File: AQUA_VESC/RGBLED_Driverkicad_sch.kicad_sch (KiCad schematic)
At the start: 12 parts, among them Q10 AO3400A, Q11 AO3401A, Q12 AO3400A, Q13 AO3401A, Q8 AO3400A, Q9 AO3401A

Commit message: AQUA VESC仮完成
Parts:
- renumbered R85 to R84, R86 to R85, R87 to R86, R88 to R87, R89 to R88, R90 to R89
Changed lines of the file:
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@@
 		(dnp no)
 		(fields_autoplaced yes)
-		(property "Reference" "#PWR0123"
+		(property "Reference" "#PWR0112"
 			(at 128.27 77.47 0)
 			(effects
@@
 			(project "AQUA_VESC"
 				(path "/8ee9fd02-9bd5-4905-927f-d8ca1179f479/3e003488-3a27-47f4-bde4-f49a514f4d8a"
-					(reference "#PWR0123")
+					(reference "#PWR0112")
 					(unit 1)
 				)
@@
 		(dnp no)
 		(fields_autoplaced yes)
-		(property "Reference" "#PWR0121"
+		(property "Reference" "#PWR0109"
 			(at 82.55 77.47 0)
 			(effects
@@
 			(project "AQUA_VESC"
 				(path "/8ee9fd02-9bd5-4905-927f-d8ca1179f479/3e003488-3a27-47f4-bde4-f49a514f4d8a"
-					(reference "#PWR0121")
+					(reference "#PWR0109")
 					(unit 1)
 				)
@@
 		(dnp no)
 		(fields_autoplaced yes)
-		(property "Reference" "R85"
+		(property "Reference" "R84"
 			(at 43.18 63.4999 0)
 			(effects
@@
 			(project "AQUA_VESC"
 				(path "/8ee9fd02-9bd5-4905-927f-d8ca1179f479/3e003488-3a27-47f4-bde4-f49a514f4d8a"
-					(reference "R85")
+					(reference "R84")
 					(unit 1)
 				)
@@
 		(dnp no)
 		(fields_autoplaced yes)
-		(property "Reference" "R88"
+		(property "Reference" "R87"
 			(at 92.71 44.4499 0)
 			(effects
@@
 			(project "AQUA_VESC"
 				(path "/8ee9fd02-9bd5-4905-927f-d8ca1179f479/3e003488-3a27-47f4-bde4-f49a514f4d8a"
-					(reference "R88")
+					(reference "R87")
 					(unit 1)
 				)
@@
 		(dnp no)
 		(fields_autoplaced yes)
-		(property "Reference" "#PWR0113"
+		(property "Reference" "#PWR0107"
 			(at 48.26 41.91 0)
 			(effects
@@
 			(project "AQUA_VESC"
 				(path "/8ee9fd02-9bd5-4905-927f-d8ca1179f479/3e003488-3a27-47f4-bde4-f49a514f4d8a"
-					(reference "#PWR0113")
+					(reference "#PWR0107")
 					(unit 1)
 				)
@@
 		(dnp no)
 		(fields_autoplaced yes)
-		(property "Reference" "#PWR0117"
+		(property "Reference" "#PWR0111"
 			(at 90.17 77.47 0)
 			(effects
@@
 			(project "AQUA_VESC"
 				(path "/8ee9fd02-9bd5-4905-927f-d8ca1179f479/3e003488-3a27-47f4-bde4-f49a514f4d8a"
-					(reference "#PWR0117")
+					(reference "#PWR0111")
 					(unit 1)
 				)
@@
 		(dnp no)
 		(fields_autoplaced yes)
-		(property "Reference" "#PWR0120"
+		(property "Reference" "#PWR0114"
 			(at 135.89 77.47 0)
 			(effects
@@
 			(project "AQUA_VESC"
 				(path "/8ee9fd02-9bd5-4905-927f-d8ca1179f479/3e003488-3a27-47f4-bde4-f49a514f4d8a"
-					(reference "#PWR0120")
+					(reference "#PWR0114")
 					(unit 1)
 				)
@@
 		(dnp no)
 		(fields_autoplaced yes)
-		(property "Reference" "#PWR0122"
+		(property "Reference" "#PWR0106"
 			(at 40.64 76.2 0)
 			(effects
@@
 			(project "AQUA_VESC"
 				(path "/8ee9fd02-9bd5-4905-927f-d8ca1179f479/3e003488-3a27-47f4-bde4-f49a514f4d8a"
-					(reference "#PWR0122")
+					(reference "#PWR0106")
 					(unit 1)
 				)
@@
 		(dnp no)
 		(fields_autoplaced yes)
-		(property "Reference" "#PWR0114"
+		(property "Reference" "#PWR0108"
 			(at 48.26 76.2 0)
 			(effects
@@
 			(project "AQUA_VESC"
 				(path "/8ee9fd02-9bd5-4905-927f-d8ca1179f479/3e003488-3a27-47f4-bde4-f49a514f4d8a"
-					(reference "#PWR0114")
+					(reference "#PWR0108")
 					(unit 1)
 				)
@@
 		(dnp no)
 		(fields_autoplaced yes)
-		(property "Reference" "R86"
+		(property "Reference" "R85"
 			(at 50.8 43.1799 0)
 			(effects
@@
 			(project "AQUA_VESC"
 				(path "/8ee9fd02-9bd5-4905-927f-d8ca1179f479/3e003488-3a27-47f4-bde4-f49a514f4d8a"
-					(reference "R86")
+					(reference "R85")
 					(unit 1)
 				)
@@
 		(dnp no)
 		(fields_autoplaced yes)
-		(property "Reference" "R89"
+		(property "Reference" "R88"
 			(at 130.81 64.7699 0)
 			(effects
@@
 			(project "AQUA_VESC"
 				(path "/8ee9fd02-9bd5-4905-927f-d8ca1179f479/3e003488-3a27-47f4-bde4-f49a514f4d8a"
-					(reference "R89")
+					(reference "R88")
 					(unit 1)
 				)
@@
 		(dnp no)
 		(fields_autoplaced yes)
-		(property "Reference" "#PWR0119"
+		(property "Reference" "#PWR0113"
 			(at 135.89 43.18 0)
 			(effects
@@
 			(project "AQUA_VESC"
 				(path "/8ee9fd02-9bd5-4905-927f-d8ca1179f479/3e003488-3a27-47f4-bde4-f49a514f4d8a"
-					(reference "#PWR0119")
+					(reference "#PWR0113")
 					(unit 1)
 				)
@@
 		(dnp no)
 		(fields_autoplaced yes)
-		(property "Reference" "R90"
+		(property "Reference" "R89"
 			(at 138.43 44.4499 0)
 			(effects
@@
 			(project "AQUA_VESC"
 				(path "/8ee9fd02-9bd5-4905-927f-d8ca1179f479/3e003488-3a27-47f4-bde4-f49a514f4d8a"
-					(reference "R90")
+					(reference "R89")
 					(unit 1)
 				)
@@
 		(dnp no)
 		(fields_autoplaced yes)
-		(property "Reference" "R87"
+		(property "Reference" "R86"
 			(at 85.09 64.7699 0)
 			(effects
@@
 			(project "AQUA_VESC"
 				(path "/8ee9fd02-9bd5-4905-927f-d8ca1179f479/3e003488-3a27-47f4-bde4-f49a514f4d8a"
-					(reference "R87")
+					(reference "R86")
 					(unit 1)
 				)
@@
 		(dnp no)
 		(fields_autoplaced yes)
-		(property "Reference" "#PWR0116"
+		(property "Reference" "#PWR0110"
 			(at 90.17 43.18 0)
 			(effects
@@
 			(project "AQUA_VESC"
 				(path "/8ee9fd02-9bd5-4905-927f-d8ca1179f479/3e003488-3a27-47f4-bde4-f49a514f4d8a"
-					(reference "#PWR0116")
-					(unit 1)
-				)
+					(reference "#PWR0110")
+					(unit 1)
+				)

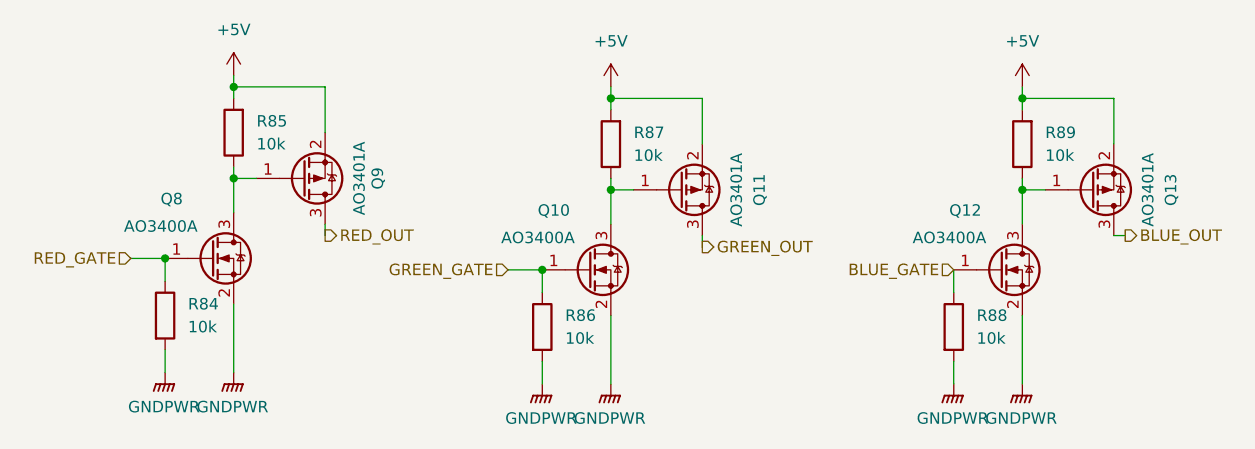
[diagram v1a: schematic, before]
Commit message: AQUA_VESC REV01作成
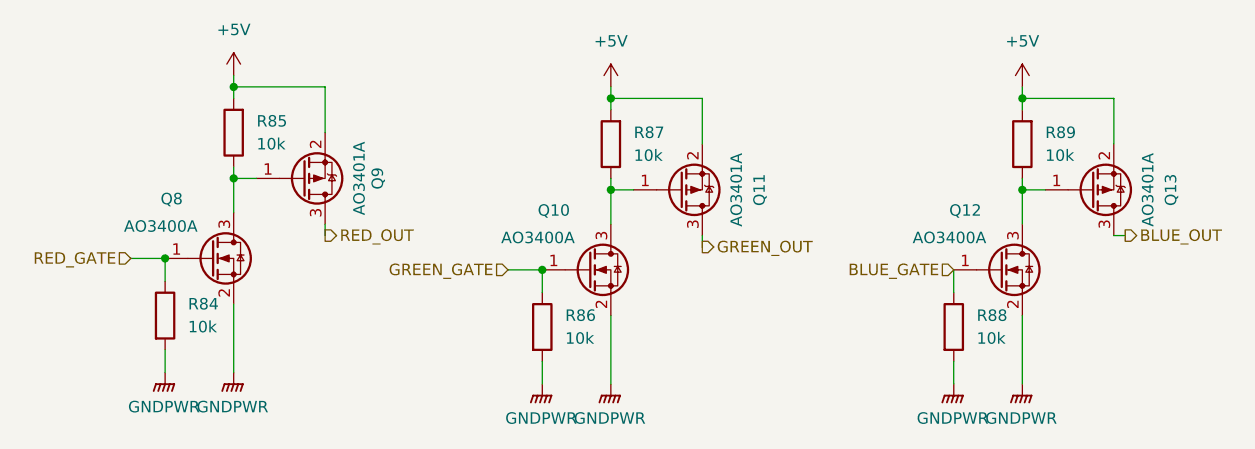
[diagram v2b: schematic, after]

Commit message: 制御基板REV01完成
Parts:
- removed Q10, Q12, Q8: AO3400A, Package_TO_SOT_SMD:SOT-23, symbol Transistor_FET:AO3400A
- added Q11, Q7, Q9: 2N7002, Package_TO_SOT_SMD:SOT-23, symbol Transistor_FET:2N7002
- renumbered Q11 to Q10, Q13 to Q12, Q9 to Q8, R84 to R68, R85 to R69, R86 to R70, R87 to R71, R88 to R72, R89 to R73
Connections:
- net BLUE_GATE: now also Q11.1 (G)
- net GNDPWR: now also Q11.2 (S), Q7.2 (S), Q9.2 (S)
- net GREEN_GATE: now also Q9.1 (G)
- net RED_GATE: now also Q7.1 (G)
- net at Q12.1 (G), R73.1: now also Q11.3 (D)
- net at Q10.1 (G), R71.1: now also Q9.3 (D)
- net at Q8.1 (G), R69.1: now also Q7.3 (D)

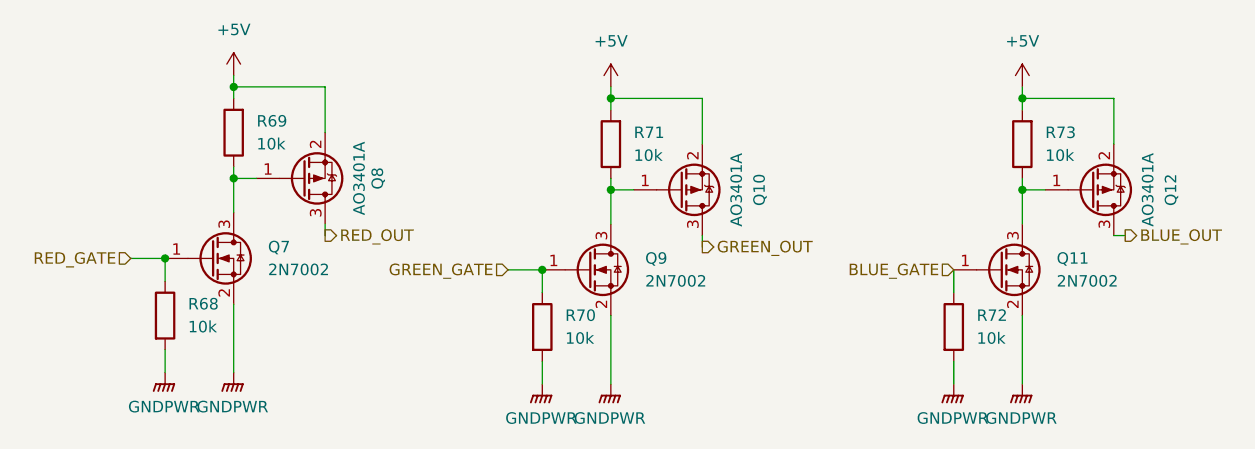
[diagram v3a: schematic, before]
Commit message: 方針変更、back_connector_escにMT60を使用しないことに
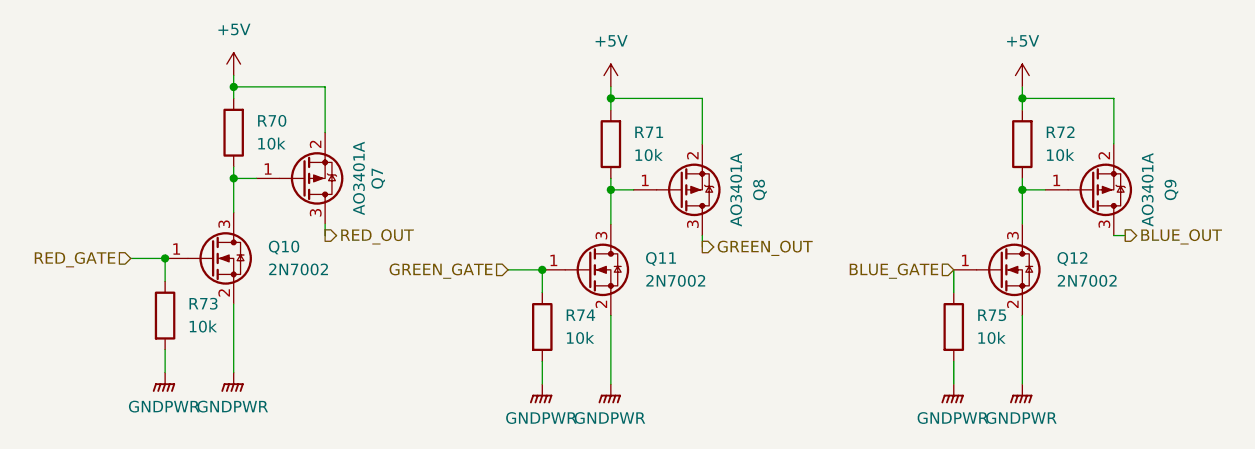
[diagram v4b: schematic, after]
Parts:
- renumbered Q7 to Q10, Q9 to Q11, Q11 to Q12, Q8 to Q7, Q10 to Q8, Q12 to Q9, R69 to R70, R73 to R72, R68 to R73, R70 to R74, R72 to R75
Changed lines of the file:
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@@
 		(on_board yes)
 		(dnp no)
-		(property "Reference" "Q12"
+		(property "Reference" "Q9"
 			(at 152.4 50.8 90)
 			(effects
@@
 			(project "AQUA_VESC"
 				(path "/8ee9fd02-9bd5-4905-927f-d8ca1179f479/3e003488-3a27-47f4-bde4-f49a514f4d8a"
-					(reference "Q12")
+					(reference "Q9")
 					(unit 1)
 				)
@@
 		(dnp no)
 		(fields_autoplaced yes)
-		(property "Reference" "#PWR095"
+		(property "Reference" "#PWR0102"
 			(at 128.27 77.47 0)
 			(effects
@@
 			(project "AQUA_VESC"
 				(path "/8ee9fd02-9bd5-4905-927f-d8ca1179f479/3e003488-3a27-47f4-bde4-f49a514f4d8a"
-					(reference "#PWR095")
+					(reference "#PWR0102")
 					(unit 1)
 				)
@@
 		(dnp no)
 		(fields_autoplaced yes)
-		(property "Reference" "Q7"
+		(property "Reference" "Q10"
 			(at 52.07 57.1499 0)
 			(effects
@@
 			(project ""
 				(path "/8ee9fd02-9bd5-4905-927f-d8ca1179f479/3e003488-3a27-47f4-bde4-f49a514f4d8a"
-					(reference "Q7")
+					(reference "Q10")
 					(unit 1)
 				)
@@
 		(dnp no)
 		(fields_autoplaced yes)
-		(property "Reference" "#PWR092"
+		(property "Reference" "#PWR0100"
 			(at 82.55 77.47 0)
 			(effects
@@
 			(project "AQUA_VESC"
 				(path "/8ee9fd02-9bd5-4905-927f-d8ca1179f479/3e003488-3a27-47f4-bde4-f49a514f4d8a"
-					(reference "#PWR092")
+					(reference "#PWR0100")
 					(unit 1)
 				)
@@
 		(dnp no)
 		(fields_autoplaced yes)
-		(property "Reference" "Q9"
+		(property "Reference" "Q11"
 			(at 93.98 58.4199 0)
 			(effects
@@
 			(project "AQUA_VESC"
 				(path "/8ee9fd02-9bd5-4905-927f-d8ca1179f479/3e003488-3a27-47f4-bde4-f49a514f4d8a"
-					(reference "Q9")
+					(reference "Q11")
 					(unit 1)
 				)
@@
 		(dnp no)
 		(fields_autoplaced yes)
-		(property "Reference" "R68"
+		(property "Reference" "R73"
 			(at 43.18 63.4999 0)
 			(effects
@@
 			(project "AQUA_VESC"
 				(path "/8ee9fd02-9bd5-4905-927f-d8ca1179f479/3e003488-3a27-47f4-bde4-f49a514f4d8a"
-					(reference "R68")
+					(reference "R73")
 					(unit 1)
 				)
@@
 		(dnp no)
 		(fields_autoplaced yes)
-		(property "Reference" "#PWR090"
+		(property "Reference" "#PWR095"
 			(at 48.26 41.91 0)
 			(effects
@@
 			(project "AQUA_VESC"
 				(path "/8ee9fd02-9bd5-4905-927f-d8ca1179f479/3e003488-3a27-47f4-bde4-f49a514f4d8a"
-					(reference "#PWR090")
+					(reference "#PWR095")
 					(unit 1)
 				)
@@
 		(dnp no)
 		(fields_autoplaced yes)
-		(property "Reference" "#PWR094"
+		(property "Reference" "#PWR0101"
 			(at 90.17 77.47 0)
 			(effects
@@
 			(project "AQUA_VESC"
 				(path "/8ee9fd02-9bd5-4905-927f-d8ca1179f479/3e003488-3a27-47f4-bde4-f49a514f4d8a"
-					(reference "#PWR094")
+					(reference "#PWR0101")
 					(unit 1)
 				)
@@
 		(dnp no)
 		(fields_autoplaced yes)
-		(property "Reference" "#PWR097"
+		(property "Reference" "#PWR0103"
 			(at 135.89 77.47 0)
 			(effects
@@
 			(project "AQUA_VESC"
 				(path "/8ee9fd02-9bd5-4905-927f-d8ca1179f479/3e003488-3a27-47f4-bde4-f49a514f4d8a"
-					(reference "#PWR097")
+					(reference "#PWR0103")
 					(unit 1)
 				)
@@
 		(dnp no)
 		(fields_autoplaced yes)
-		(property "Reference" "#PWR089"
+		(property "Reference" "#PWR098"
 			(at 40.64 76.2 0)
 			(effects
@@
 			(project "AQUA_VESC"
 				(path "/8ee9fd02-9bd5-4905-927f-d8ca1179f479/3e003488-3a27-47f4-bde4-f49a514f4d8a"
-					(reference "#PWR089")
+					(reference "#PWR098")
 					(unit 1)
 				)
@@
 		(dnp no)
 		(fields_autoplaced yes)
-		(property "Reference" "#PWR091"
+		(property "Reference" "#PWR099"
 			(at 48.26 76.2 0)
 			(effects
@@
 			(project "AQUA_VESC"
 				(path "/8ee9fd02-9bd5-4905-927f-d8ca1179f479/3e003488-3a27-47f4-bde4-f49a514f4d8a"
-					(reference "#PWR091")
+					(reference "#PWR099")
 					(unit 1)
 				)
@@
 		(dnp no)
 		(fields_autoplaced yes)
-		(property "Reference" "Q11"
+		(property "Reference" "Q12"
 			(at 139.7 58.4199 0)
 			(effects
@@
 			(project "AQUA_VESC"
 				(path "/8ee9fd02-9bd5-4905-927f-d8ca1179f479/3e003488-3a27-47f4-bde4-f49a514f4d8a"
-					(reference "Q11")
+					(reference "Q12")
 					(unit 1)
 				)
@@
 		(dnp no)
 		(fields_autoplaced yes)
-		(property "Reference" "R69"
+		(property "Reference" "R70"
 			(at 50.8 43.1799 0)
 			(effects
@@
 			(project "AQUA_VESC"
 				(path "/8ee9fd02-9bd5-4905-927f-d8ca1179f479/3e003488-3a27-47f4-bde4-f49a514f4d8a"
-					(reference "R69")
+					(reference "R70")
 					(unit 1)
 				)
@@
 		(dnp no)
 		(fields_autoplaced yes)
-		(property "Reference" "R72"
+		(property "Reference" "R75"
 			(at 130.81 64.7699 0)
 			(effects
@@
 			(project "AQUA_VESC"
 				(path "/8ee9fd02-9bd5-4905-927f-d8ca1179f479/3e003488-3a27-47f4-bde4-f49a514f4d8a"
-					(reference "R72")
+					(reference "R75")
 					(unit 1)
 				)
@@
 		(on_board yes)
 		(dnp no)
-		(property "Reference" "Q10"
+		(property "Reference" "Q8"
 			(at 106.68 50.8 90)
 			(effects
@@
 			(project "AQUA_VESC"
 				(path "/8ee9fd02-9bd5-4905-927f-d8ca1179f479/3e003488-3a27-47f4-bde4-f49a514f4d8a"
-					(reference "Q10")
+					(reference "Q8")
 					(unit 1)
 				)
@@
 		(dnp no)
 		(fields_autoplaced yes)
-		(property "Reference" "#PWR096"
+		(property "Reference" "#PWR097"
 			(at 135.89 43.18 0)
 			(effects
@@
 			(project "AQUA_VESC"
 				(path "/8ee9fd02-9bd5-4905-927f-d8ca1179f479/3e003488-3a27-47f4-bde4-f49a514f4d8a"
-					(reference "#PWR096")
+					(reference "#PWR097")
 					(unit 1)
 				)
@@
 		(dnp no)
 		(fields_autoplaced yes)
-		(property "Reference" "R73"
+		(property "Reference" "R72"
 			(at 138.43 44.4499 0)
 			(effects
@@
 			(project "AQUA_VESC"
 				(path "/8ee9fd02-9bd5-4905-927f-d8ca1179f479/3e003488-3a27-47f4-bde4-f49a514f4d8a"
-					(reference "R73")
+					(reference "R72")
 					(unit 1)
 				)
@@
 		(dnp no)
 		(fields_autoplaced yes)
-		(property "Reference" "R70"
+		(property "Reference" "R74"
 			(at 85.09 64.7699 0)
 			(effects
@@
 			(project "AQUA_VESC"
 				(path "/8ee9fd02-9bd5-4905-927f-d8ca1179f479/3e003488-3a27-47f4-bde4-f49a514f4d8a"
-					(reference "R70")
+					(reference "R74")
 					(unit 1)
 				)
@@
 		(on_board yes)
 		(dnp no)
-		(property "Reference" "Q8"
+		(property "Reference" "Q7"
 			(at 64.262 49.53 90)
 			(effects
@@
 			(project "AQUA_VESC"
 				(path "/8ee9fd02-9bd5-4905-927f-d8ca1179f479/3e003488-3a27-47f4-bde4-f49a514f4d8a"
-					(reference "Q8")
+					(reference "Q7")
 					(unit 1)
 				)
@@
 		(dnp no)
 		(fields_autoplaced yes)
-		(property "Reference" "#PWR093"
+		(property "Reference" "#PWR096"
 			(at 90.17 43.18 0)
 			(effects
@@
 			(project "AQUA_VESC"
 				(path "/8ee9fd02-9bd5-4905-927f-d8ca1179f479/3e003488-3a27-47f4-bde4-f49a514f4d8a"
-					(reference "#PWR093")
-					(unit 1)
-				)
+					(reference "#PWR096")
+					(unit 1)
+				)
